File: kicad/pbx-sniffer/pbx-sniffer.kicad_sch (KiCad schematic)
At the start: 1 part

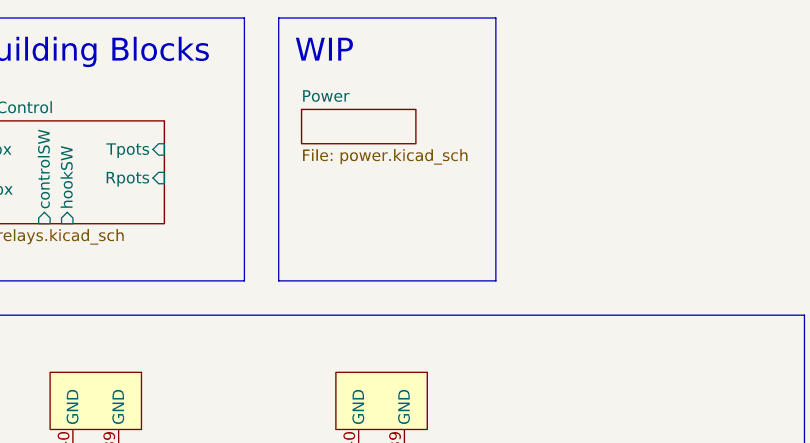
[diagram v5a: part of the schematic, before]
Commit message: remove old power sheet
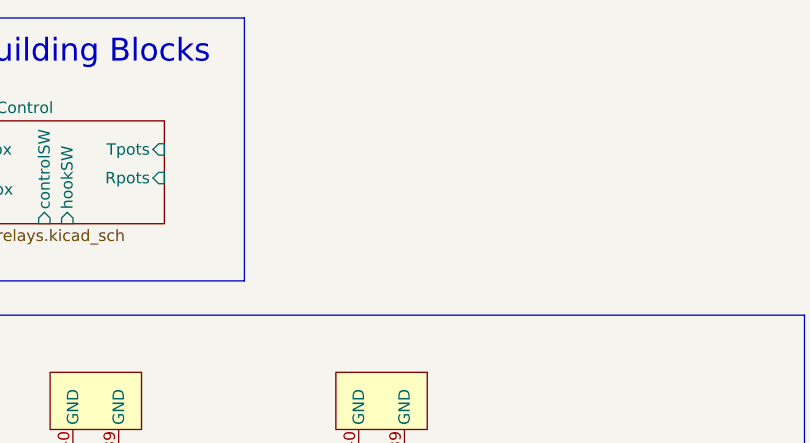
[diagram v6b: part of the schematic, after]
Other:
- removed sheet Power
- note removed: "WIP"
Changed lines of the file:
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@@
 	)
 	(rectangle
-		(start 321.31 16.51)
-		(end 345.44 45.72)
-		(stroke
-			(width 0)
-			(type default)
-		)
-		(fill
-			(type none)
-		)
-	)
-	(rectangle
 		(start 264.16 49.53)
 		(end 379.73 184.15)
@@
 		)
 	)
-	(text "WIP\n"
-		(exclude_from_sim no)
-		(at 326.39 20.32 0)
-		(effects
-			(font
-				(size 2.54 2.54)
-			)
-		)
-	)
 	(text "Telephony IO & Sniffing"
 		(exclude_from_sim no)
@@
 				)
 			)
-		)
-	)
-	(sheet
-		(at 323.85 26.67)
-		(size 12.7 3.81)
-		(exclude_from_sim no)
-		(in_bom no)
-		(on_board no)
-		(dnp no)
-		(fields_autoplaced yes)
-		(stroke
-			(width 0.1524)
-			(type solid)
-		)
-		(fill
-			(color 0 0 0 0.0000)
-		)
-		(property "Sheetname" "Power"
-			(at 323.85 25.9584 0)
-			(effects
-				(font
-					(size 1.27 1.27)
-				)
-				(justify left bottom)
-			)
-		)
-		(property "Sheetfile" "power.kicad_sch"
-			(at 323.85 31.0646 0)
-			(effects
-				(font
-					(size 1.27 1.27)
-				)
-				(justify left top)
-			)
-		)
-		(instances
-			(project "pbx-sniffer"
-				(path "/4a5b9b8a-323a-4796-bf73-ccba532d2e31"
-					(page "4")
-				)
-			)

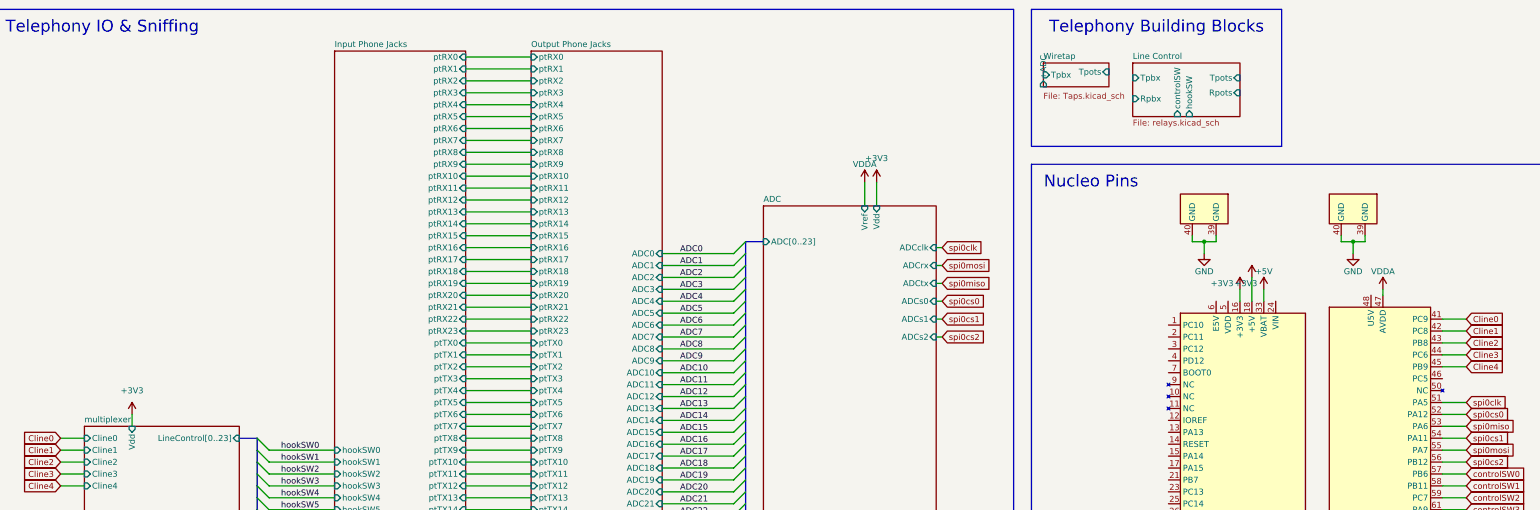
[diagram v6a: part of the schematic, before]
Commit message: start adding shift registers for signalling
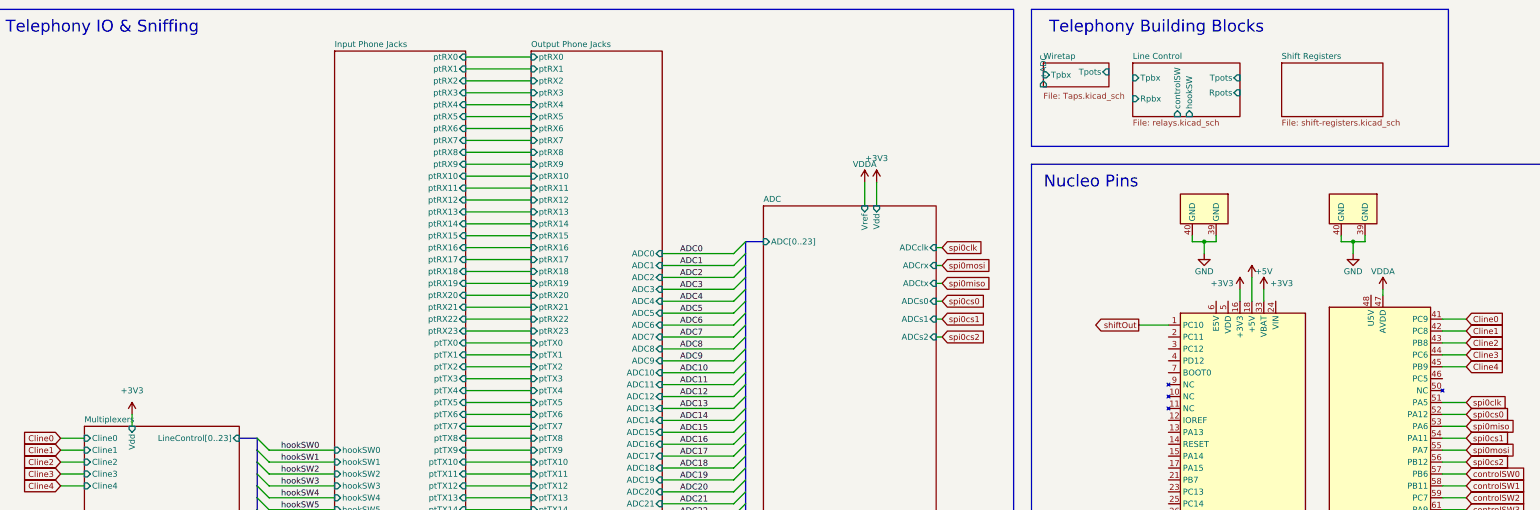
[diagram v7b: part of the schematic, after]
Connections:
- net shiftOut: now reaches U1.1 (PC10)
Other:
- sheet multiplexer renamed Multiplexers
- added sheet Shift Registers (shift-registers.kicad_sch)
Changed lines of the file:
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@@
 	(rectangle
 		(start 264.16 16.51)
-		(end 317.5 45.72)
+		(end 353.06 45.72)
 		(stroke
 			(width 0)
@@
 	(wire
 		(pts
+			(xy 287.02 83.82) (xy 293.37 83.82)
+		)
+		(stroke
+			(width 0)
+			(type default)
+		)
+	)
+	(wire
+		(pts
 			(xy 143.51 171.45) (xy 157.48 171.45)
 		)
@@
 		)
 	)
+	(global_label "shiftOut"
+		(shape output)
+		(at 287.02 83.82 180)
+		(fields_autoplaced yes)
+		(effects
+			(font
+				(size 1.27 1.27)
+			)
+			(justify right)
+		)
+		(property "Intersheetrefs" "${INTERSHEET_REFS}"
+			(at 276.5963 83.82 0)
+			(effects
+				(font
+					(size 1.27 1.27)
+				)
+				(justify right)
+				(hide yes)
+			)
+		)
+	)
 	(global_label "controlSW1"
 		(shape input)
@@
 		)
 		(property "Value" "+3V3"
-			(at 309.88 74.93 0)
+			(at 317.5 74.93 0)
 			(effects
 				(font
@@
 	)
 	(sheet
+		(at 317.5 27.94)
+		(size 21.59 11.43)
+		(exclude_from_sim no)
+		(in_bom yes)
+		(on_board yes)
+		(dnp no)
+		(fields_autoplaced yes)
+		(stroke
+			(width 0.1524)
+			(type solid)
+		)
+		(fill
+			(color 0 0 0 0.0000)
+		)
+		(property "Sheetname" "Shift Registers"
+			(at 317.5 27.2284 0)
+			(effects
+				(font
+					(size 1.27 1.27)
+				)
+				(justify left bottom)
+			)
+		)
+		(property "Sheetfile" "shift-registers.kicad_sch"
+			(at 317.5 39.9546 0)
+			(effects
+				(font
+					(size 1.27 1.27)
+				)
+				(justify left top)
+			)
+		)
+		(instances
+			(project "pbx-sniffer"
+				(path "/4a5b9b8a-323a-4796-bf73-ccba532d2e31"
+					(page "56")
+				)
+			)
+		)
+	)
+	(sheet
 		(at 115.57 25.4)
 		(size 27.94 246.38)
@@
 			(color 0 0 0 0.0000)
 		)
-		(property "Sheetname" "multiplexer"
+		(property "Sheetname" "Multiplexers"
 			(at 62.23 104.6984 0)
 			(effects
